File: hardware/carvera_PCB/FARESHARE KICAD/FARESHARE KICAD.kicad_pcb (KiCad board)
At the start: 2 copper layers, 70 x 55 mm, 14 parts, among them J1 0022232041, J2 0022232041, J3 0022232041, J4 22-23-2021, J5 PJ-102A

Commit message: changed power footprint
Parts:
- J5: footprint digikey-footprints:Barrel_Jack_5.5mmODx2.1mmID_PJ-102A -> digikey-footprints:Barrel_Jack_5.5mmODx2.1mmID_PJ-202A
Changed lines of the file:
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@@
 		(descr "http://www.molex.com/pdm_docs/sd/022232031_sd.pdf")
 		(property "Reference" "J3"
-			(at 2 -4.56 360)
+			(at 2 -4.56 0)
 			(layer "F.SilkS")
 			(effects
@@
 		)
 		(property "Value" "0022232041"
-			(at 4.08 4.52 360)
+			(at 4.08 4.52 0)
 			(layer "F.Fab")
 			(effects
@@
 		)
 		(fp_text user "${REFERENCE}"
-			(at 4.17 0 360)
+			(at 4.17 0 0)
 			(layer "F.Fab")
 			(effects
@@
 		(descr "http://www.te.com/commerce/DocumentDelivery/DDEController?Action=srchrtrv&DocNm=1825910&DocType=Customer+Drawing&DocLang=English")
 		(property "Reference" "S1"
-			(at 3.81 -2.3368 270)
+			(at 3.81 -2.3368 -90)
 			(layer "F.SilkS")
 			(effects
@@
 		)
 		(property "Value" "1825910-6"
-			(at 3.6322 7.0866 270)
+			(at 3.6322 7.0866 -90)
 			(layer "F.Fab")
 			(effects
@@
 		)
 		(fp_text user "${REFERENCE}"
-			(at 3.3782 2.286 270)
+			(at 3.3782 2.286 -90)
 			(layer "F.Fab")
 			(effects
@@
 		(descr "http://www.molex.com/pdm_docs/sd/022232031_sd.pdf")
 		(property "Reference" "J4"
-			(at 1.45 -4.48 360)
+			(at 1.45 -4.48 0)
 			(layer "F.SilkS")
 			(effects
@@
 		)
 		(property "Value" "22-23-2021"
-			(at 1.23 4.72 360)
+			(at 1.23 4.72 0)
 			(layer "F.Fab")
 			(effects
@@
 		)
 		(fp_text user "${REFERENCE}"
-			(at 1.25 0.03 360)
+			(at 1.25 0.03 0)
 			(layer "F.Fab")
 			(effects
@@
 		)
 	)
-	(footprint "digikey-footprints:Barrel_Jack_5.5mmODx2.1mmID_PJ-102A"
+	(footprint "digikey-footprints:Barrel_Jack_5.5mmODx2.1mmID_PJ-202A"
 		(layer "F.Cu")
 		(at 92.5 56.5 90)
 		(property "Reference" "J5"
-			(at 5.5 5.5 270)
+			(at 0 -12.1 90)
 			(layer "F.SilkS")
 			(effects
@@
 		)
 		(property "Value" "PJ-102A"
-			(at 0 5.8 270)
+			(at 0 5.8 90)
 			(layer "F.Fab")
 			(effects
@@
 			)
 		)
-		(property "Footprint" "digikey-footprints:Barrel_Jack_5.5mmODx2.1mmID_PJ-102A"
+		(property "Footprint" "digikey-footprints:Barrel_Jack_5.5mmODx2.1mmID_PJ-202A"
 			(at 0 0 90)
 			(unlocked yes)
@@
 		)
 		(fp_line
-			(start 4.8 -10.95)
-			(end 4.8 4.25)
+			(start 4.8 -11)
+			(end 4.8 4.2)
 			(stroke
 				(width 0.05)
@@
 		)
 		(fp_line
-			(start -5.9 -10.95)
-			(end 4.8 -10.95)
+			(start -5.9 -11)
+			(end 4.8 -11)
 			(stroke
 				(width 0.05)
@@
 		)
 		(fp_line
-			(start -5.9 -10.95)
-			(end -5.9 4.25)
+			(start -5.9 -11)
+			(end -5.9 4.2)
 			(stroke
 				(width 0.05)
@@
 		)
 		(fp_line
-			(start -5.9 4.25)
-			(end 4.8 4.25)
+			(start -5.9 4.2)
+			(end 4.8 4.2)
 			(stroke
 				(width 0.05)
@@
 		(pad "1" thru_hole rect
 			(at 0 3 90)
-			(size 2.6 2)
-			(drill oval 1.6 1)
+			(size 4.5 2)
+			(drill oval 3.5 1)
 			(layers "*.Cu" "*.Mask")
 			(remove_unused_layers no)
@@
 		(pad "2" thru_hole rect
 			(at 0 -3 90)
-			(size 2.6 2)
-			(drill oval 1.6 1)
+			(size 4.5 2)
+			(drill oval 3.5 1)
 			(layers "*.Cu" "*.Mask")
 			(remove_unused_layers no)
@@
 		(pad "3" thru_hole rect
 			(at -4.7 0 90)
-			(size 2 2.6)
-			(drill oval 1 1.6)
+			(size 2 4.5)
+			(drill oval 1 3.5)
 			(layers "*.Cu" "*.Mask")
 			(remove_unused_layers no)
@@
 	)
 	(segment
-		(start 104.044888 56.544888)
-		(end 104 56.5)
+		(start 104 56.5)
+		(end 127 56.5)
 		(width 1.5)
 		(layer "F.Cu")
@@
 	)
 	(segment
-		(start 104 56.5)
-		(end 127 56.5)
+		(start 104.044888 61)
+		(end 104.044888 56.544888)
 		(width 1.5)
 		(layer "F.Cu")
@@
 	)
 	(segment
-		(start 104.044888 61)
+		(start 104 56.5)
 		(end 104.044888 56.544888)
 		(width 1.5)

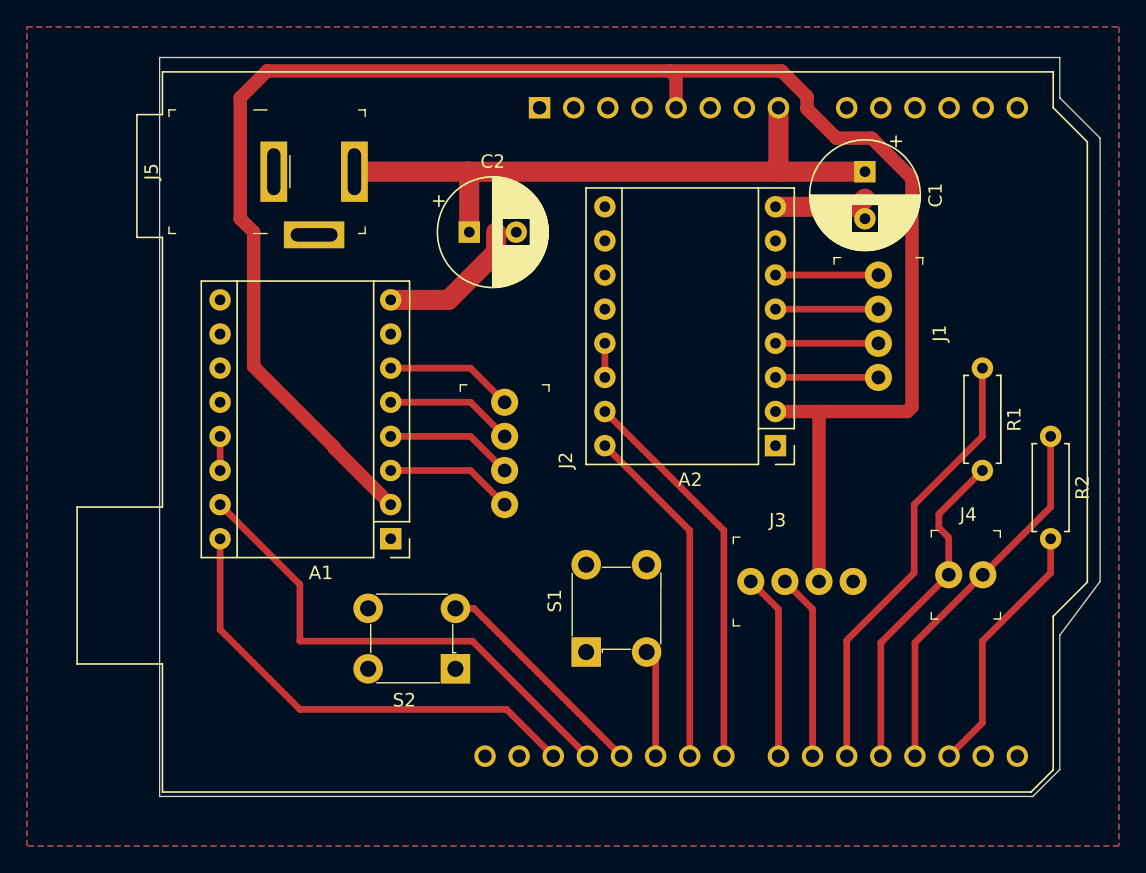
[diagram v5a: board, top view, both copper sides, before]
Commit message: trying to use edge cut to cut slots
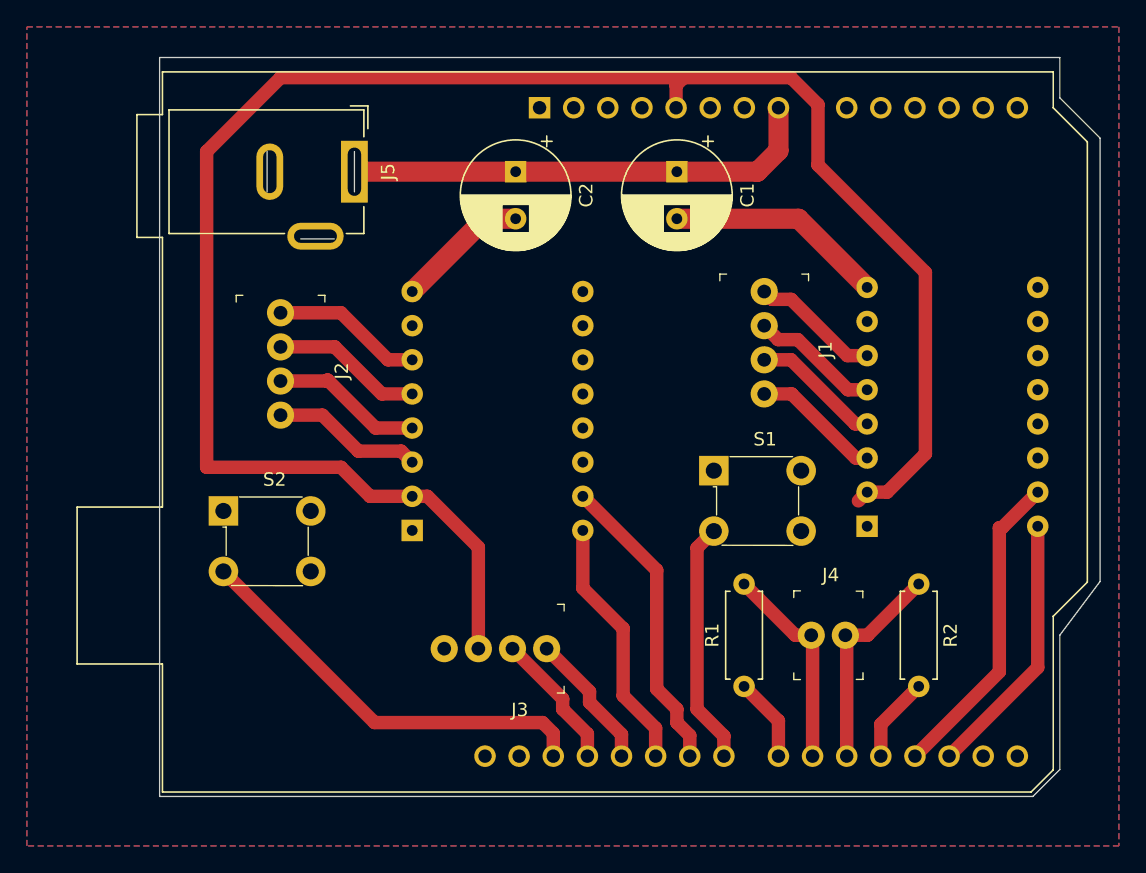
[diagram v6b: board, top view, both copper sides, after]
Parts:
- A1, A2: moved to B.Cu
- J5: value PJ-102A -> Barrel_Jack_Switch_Pin3Ring; footprint digikey-footprints:Barrel_Jack_5.5mmODx2.1mmID_PJ-202A -> Connector_BarrelJack:BarrelJack_GCT_DCJ200-10-A_Horizontal
- moved R1 29.6 mm to (124.5, 94.8), turned to 90 degrees
- moved S2 20.9 mm to (85.8, 81.8), turned to 0 degrees
- moved J2 18.0 mm to (90.0, 67.0)
- moved S1 16.5 mm to (122.2, 78.8), turned to 0 degrees
- moved J3 16.0 mm to (109.8, 92.0), turned to 180 degrees
- moved R2 14.7 mm to (137.5, 87.2)
- moved C1 14.0 mm to (119.5, 56.5)
- moved J4 11.2 mm to (129.5, 91.0)
- moved A2 9.08 mm to (133.7, 82.9), turned to 0 degrees
- moved J1 8.59 mm to (126.0, 65.4)
- moved C2 5.67 mm to (107.5, 56.5), turned to -90 degrees
- moved J5 3.00 mm to (95.5, 56.5), turned to -90 degrees
- moved A1 1.72 mm to (99.8, 83.2), turned to 0 degrees
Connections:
- A1 pad 15: D12 -> D9
- A1 pad 16: D13 -> D10
- A2 pad 15: D8 -> D3
- A2 pad 16: D9 -> D2
- J3 pad 1: D7 -> D11
- J3 pad 2: D6 -> D12
- J4 pad 1: D4 -> D6
- J4 pad 2: D3 -> D5
- R1 pad 1: D5 -> D7
- R1 pad 2: D4 -> D6
- R2 pad 1: D3 -> D5
- R2 pad 2: D2 -> D4
- S1 pad 3: D10 -> D8
- S2 pad 3: D11 -> D13
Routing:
- net D12: track 37.6 -> 10.3 mm
- net D4: track 25.0 -> 6.36 mm
- net D5: track 33.1 -> 16.1 mm
- net +12V: track 47.3 -> 35.5 mm
- net D8: track 29.3 -> 18.1 mm
- net D10: track 8.03 -> 19.0 mm
- net Net-(A2-VMOT): track 6.91 -> 16.3 mm
- net +5V: track 133.0 -> 140.6 mm
- net D7: track 13.9 -> 6.25 mm
- net D11: track 16.9 -> 10.3 mm
- net D3: track 28.1 -> 23.6 mm
- net D13: track 35.5 -> 31.2 mm
- net D9: track 25.7 -> 22.6 mm
- net Net-(A2-~{RESET}): track 2.54 -> 0.00 mm
- net Net-(A1-~{RESET}): track 2.54 -> 0.00 mm
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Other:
- outline, holes or cut-outs redrawn
